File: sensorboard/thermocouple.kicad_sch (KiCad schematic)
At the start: 8 parts, among them U4 MAX31856

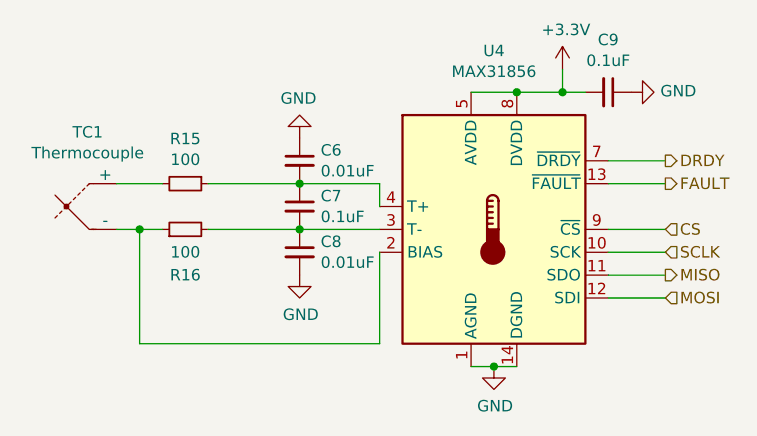
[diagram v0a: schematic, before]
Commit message: Stackup + capacitor fps
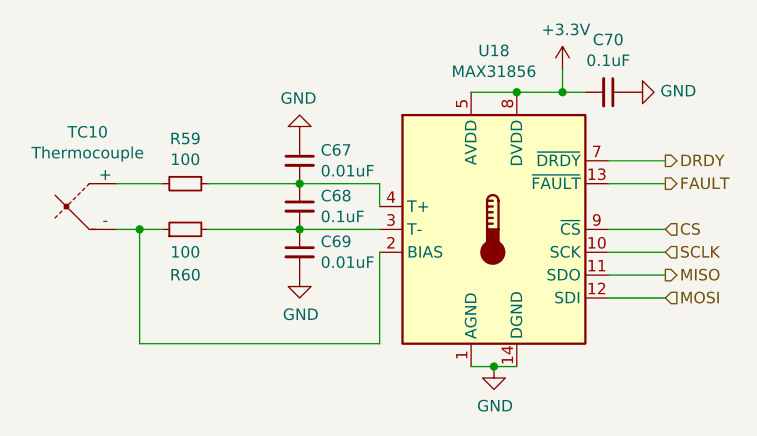
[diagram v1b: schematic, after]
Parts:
- renumbered C6 to C67, C7 to C68, C8 to C69, C9 to C70, R15 to R59, R16 to R60, TC1 to TC10, U4 to U18
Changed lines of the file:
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@@
   (symbol (lib_id "Sensor_Temperature:MAX31856") (at 95.25 73.66 0)
     (in_bom yes) (on_board yes)
-    (property "Reference" "U4" (id 0) (at 95.25 53.8226 0))
+    (property "Reference" "U18" (id 0) (at 95.25 53.8226 0))
     (property "Value" "MAX31856" (id 1) (at 95.25 56.134 0))
     (property "Footprint" "Package_SO:TSSOP-14_4.4x5mm_P0.65mm" (id 2) (at 99.06 87.63 0)
@@
   (symbol (lib_id "power:GND") (at 95.25 88.9 0)
     (in_bom yes) (on_board yes)
-    (property "Reference" "#PWR026" (id 0) (at 95.25 95.25 0)
+    (property "Reference" "#PWR0130" (id 0) (at 95.25 95.25 0)
       (effects (font (size 1.27 1.27)) hide)
     )
@@
   (symbol (lib_id "analogue-cache:+3.3V") (at 102.87 55.88 0)
     (in_bom yes) (on_board yes)
-    (property "Reference" "#PWR028" (id 0) (at 102.87 59.69 0)
+    (property "Reference" "#PWR0131" (id 0) (at 102.87 59.69 0)
       (effects (font (size 1.27 1.27)) hide)
     )
@@
   (symbol (lib_id "Device:C_Small") (at 107.95 58.42 270)
     (in_bom yes) (on_board yes)
-    (property "Reference" "C9" (id 0) (at 107.95 52.6034 90))
+    (property "Reference" "C70" (id 0) (at 107.95 52.6034 90))
     (property "Value" "0.1uF" (id 1) (at 107.95 54.9148 90))
     (property "Footprint" "Capacitor_SMD:C_0603_1608Metric" (id 2) (at 107.95 58.42 0)
@@
   (symbol (lib_id "power:GND") (at 110.49 58.42 90)
     (in_bom yes) (on_board yes)
-    (property "Reference" "#PWR029" (id 0) (at 116.84 58.42 0)
+    (property "Reference" "#PWR0132" (id 0) (at 116.84 58.42 0)
       (effects (font (size 1.27 1.27)) hide)
     )
@@
   (symbol (lib_id "Device:Thermocouple") (at 50.8 71.12 0)
     (in_bom yes) (on_board yes)
-    (property "Reference" "TC1" (id 0) (at 50.1142 62.865 0))
+    (property "Reference" "TC10" (id 0) (at 50.1142 62.865 0))
     (property "Value" "Thermocouple" (id 1) (at 50.1142 65.1764 0))
     (property "Footprint" "TerminalBlock_TE-Connectivity:TerminalBlock_TE_282834-2_1x02_P2.54mm_Horizontal" (id 2) (at 36.195 69.85 0)
@@
   (symbol (lib_id "Device:R_Small") (at 60.96 68.58 270)
     (in_bom yes) (on_board yes)
-    (property "Reference" "R15" (id 0) (at 60.96 63.6016 90))
+    (property "Reference" "R59" (id 0) (at 60.96 63.6016 90))
     (property "Value" "100" (id 1) (at 60.96 65.913 90))
     (property "Footprint" "Resistor_SMD:R_0603_1608Metric" (id 2) (at 60.96 68.58 0)
@@
   (symbol (lib_id "Device:R_Small") (at 60.96 73.66 90)
     (in_bom yes) (on_board yes)
-    (property "Reference" "R16" (id 0) (at 60.96 78.74 90))
+    (property "Reference" "R60" (id 0) (at 60.96 78.74 90))
     (property "Value" "100" (id 1) (at 60.96 76.2 90))
     (property "Footprint" "Resistor_SMD:R_0603_1608Metric" (id 2) (at 60.96 73.66 0)
@@
   (symbol (lib_id "Device:C_Small") (at 73.66 71.12 0)
     (in_bom yes) (on_board yes)
-    (property "Reference" "C7" (id 0) (at 75.9968 69.9516 0)
+    (property "Reference" "C68" (id 0) (at 75.9968 69.9516 0)
       (effects (font (size 1.27 1.27)) (justify left))
     )
@@
   (symbol (lib_id "Device:C_Small") (at 73.66 66.04 0)
     (in_bom yes) (on_board yes)
-    (property "Reference" "C6" (id 0) (at 75.9968 64.8716 0)
+    (property "Reference" "C67" (id 0) (at 75.9968 64.8716 0)
       (effects (font (size 1.27 1.27)) (justify left))
     )
@@
   (symbol (lib_id "Device:C_Small") (at 73.66 76.2 0)
     (in_bom yes) (on_board yes)
-    (property "Reference" "C8" (id 0) (at 75.9968 75.0316 0)
+    (property "Reference" "C69" (id 0) (at 75.9968 75.0316 0)
       (effects (font (size 1.27 1.27)) (justify left))
     )
@@
   (symbol (lib_id "power:GND") (at 73.66 78.74 0)
     (in_bom yes) (on_board yes)
-    (property "Reference" "#PWR025" (id 0) (at 73.66 85.09 0)
+    (property "Reference" "#PWR0129" (id 0) (at 73.66 85.09 0)
       (effects (font (size 1.27 1.27)) hide)
     )
@@
   (symbol (lib_id "power:GND") (at 73.66 63.5 180)
     (in_bom yes) (on_board yes)
-    (property "Reference" "#PWR024" (id 0) (at 73.66 57.15 0)
+    (property "Reference" "#PWR0128" (id 0) (at 73.66 57.15 0)
       (effects (font (size 1.27 1.27)) hide)
     )

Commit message: boost converter fixed
rearrangement of coaxial connector line and gnd stitching
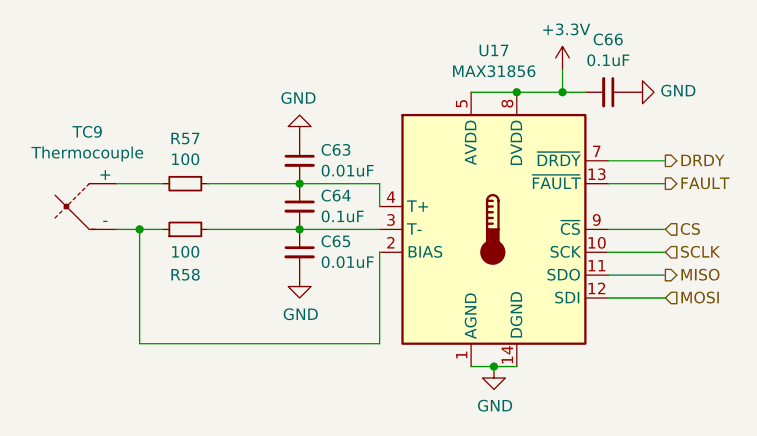
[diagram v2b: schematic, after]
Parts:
- renumbered C67 to C63, C68 to C64, C69 to C65, C70 to C66, R59 to R57, R60 to R58, TC10 to TC9, U18 to U17
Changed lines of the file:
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@@
   (symbol (lib_id "Sensor_Temperature:MAX31856") (at 95.25 73.66 0)
     (in_bom yes) (on_board yes)
-    (property "Reference" "U18" (id 0) (at 95.25 53.8226 0))
+    (property "Reference" "U17" (id 0) (at 95.25 53.8226 0))
     (property "Value" "MAX31856" (id 1) (at 95.25 56.134 0))
     (property "Footprint" "Package_SO:TSSOP-14_4.4x5mm_P0.65mm" (id 2) (at 99.06 87.63 0)
@@
   (symbol (lib_id "power:GND") (at 95.25 88.9 0)
     (in_bom yes) (on_board yes)
-    (property "Reference" "#PWR0130" (id 0) (at 95.25 95.25 0)
+    (property "Reference" "#PWR0125" (id 0) (at 95.25 95.25 0)
       (effects (font (size 1.27 1.27)) hide)
     )
@@
   (symbol (lib_id "analogue-cache:+3.3V") (at 102.87 55.88 0)
     (in_bom yes) (on_board yes)
-    (property "Reference" "#PWR0131" (id 0) (at 102.87 59.69 0)
+    (property "Reference" "#PWR0126" (id 0) (at 102.87 59.69 0)
       (effects (font (size 1.27 1.27)) hide)
     )
@@
   (symbol (lib_id "Device:C_Small") (at 107.95 58.42 270)
     (in_bom yes) (on_board yes)
-    (property "Reference" "C70" (id 0) (at 107.95 52.6034 90))
+    (property "Reference" "C66" (id 0) (at 107.95 52.6034 90))
     (property "Value" "0.1uF" (id 1) (at 107.95 54.9148 90))
     (property "Footprint" "Capacitor_SMD:C_0603_1608Metric" (id 2) (at 107.95 58.42 0)
@@
   (symbol (lib_id "power:GND") (at 110.49 58.42 90)
     (in_bom yes) (on_board yes)
-    (property "Reference" "#PWR0132" (id 0) (at 116.84 58.42 0)
+    (property "Reference" "#PWR0127" (id 0) (at 116.84 58.42 0)
       (effects (font (size 1.27 1.27)) hide)
     )
@@
   (symbol (lib_id "Device:Thermocouple") (at 50.8 71.12 0)
     (in_bom yes) (on_board yes)
-    (property "Reference" "TC10" (id 0) (at 50.1142 62.865 0))
+    (property "Reference" "TC9" (id 0) (at 50.1142 62.865 0))
     (property "Value" "Thermocouple" (id 1) (at 50.1142 65.1764 0))
     (property "Footprint" "TerminalBlock_TE-Connectivity:TerminalBlock_TE_282834-2_1x02_P2.54mm_Horizontal" (id 2) (at 36.195 69.85 0)
@@
   (symbol (lib_id "Device:R_Small") (at 60.96 68.58 270)
     (in_bom yes) (on_board yes)
-    (property "Reference" "R59" (id 0) (at 60.96 63.6016 90))
+    (property "Reference" "R57" (id 0) (at 60.96 63.6016 90))
     (property "Value" "100" (id 1) (at 60.96 65.913 90))
     (property "Footprint" "Resistor_SMD:R_0603_1608Metric" (id 2) (at 60.96 68.58 0)
@@
   (symbol (lib_id "Device:R_Small") (at 60.96 73.66 90)
     (in_bom yes) (on_board yes)
-    (property "Reference" "R60" (id 0) (at 60.96 78.74 90))
+    (property "Reference" "R58" (id 0) (at 60.96 78.74 90))
     (property "Value" "100" (id 1) (at 60.96 76.2 90))
     (property "Footprint" "Resistor_SMD:R_0603_1608Metric" (id 2) (at 60.96 73.66 0)
@@
   (symbol (lib_id "Device:C_Small") (at 73.66 71.12 0)
     (in_bom yes) (on_board yes)
-    (property "Reference" "C68" (id 0) (at 75.9968 69.9516 0)
+    (property "Reference" "C64" (id 0) (at 75.9968 69.9516 0)
       (effects (font (size 1.27 1.27)) (justify left))
     )
@@
   (symbol (lib_id "Device:C_Small") (at 73.66 66.04 0)
     (in_bom yes) (on_board yes)
-    (property "Reference" "C67" (id 0) (at 75.9968 64.8716 0)
+    (property "Reference" "C63" (id 0) (at 75.9968 64.8716 0)
       (effects (font (size 1.27 1.27)) (justify left))
     )
@@
   (symbol (lib_id "Device:C_Small") (at 73.66 76.2 0)
     (in_bom yes) (on_board yes)
-    (property "Reference" "C69" (id 0) (at 75.9968 75.0316 0)
+    (property "Reference" "C65" (id 0) (at 75.9968 75.0316 0)
       (effects (font (size 1.27 1.27)) (justify left))
     )
@@
   (symbol (lib_id "power:GND") (at 73.66 78.74 0)
     (in_bom yes) (on_board yes)
-    (property "Reference" "#PWR0129" (id 0) (at 73.66 85.09 0)
+    (property "Reference" "#PWR0124" (id 0) (at 73.66 85.09 0)
       (effects (font (size 1.27 1.27)) hide)
     )
@@
   (symbol (lib_id "power:GND") (at 73.66 63.5 180)
     (in_bom yes) (on_board yes)
-    (property "Reference" "#PWR0128" (id 0) (at 73.66 57.15 0)
+    (property "Reference" "#PWR0123" (id 0) (at 73.66 57.15 0)
       (effects (font (size 1.27 1.27)) hide)
     )

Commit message: Changed pins for CAN lines and removed LED
need to rearrange LNA_IN line for less interference
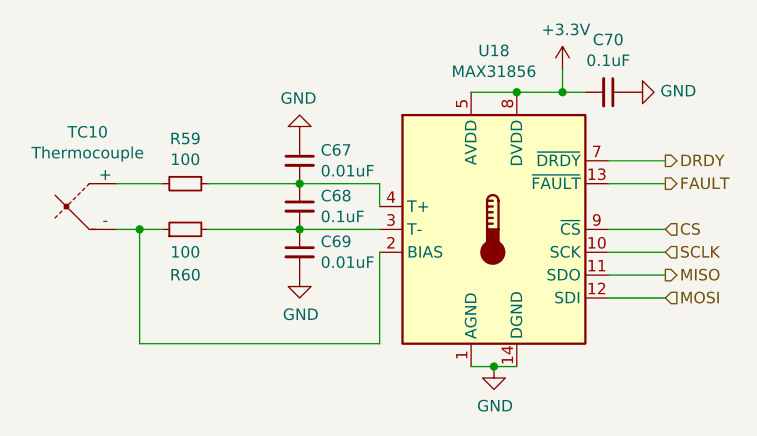
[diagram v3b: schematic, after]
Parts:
- renumbered C63 to C67, C64 to C68, C65 to C69, C66 to C70, R57 to R59, R58 to R60, TC9 to TC10, U17 to U18
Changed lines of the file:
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@@
   (symbol (lib_id "Sensor_Temperature:MAX31856") (at 95.25 73.66 0)
     (in_bom yes) (on_board yes)
-    (property "Reference" "U17" (id 0) (at 95.25 53.8226 0))
+    (property "Reference" "U18" (id 0) (at 95.25 53.8226 0))
     (property "Value" "MAX31856" (id 1) (at 95.25 56.134 0))
     (property "Footprint" "Package_SO:TSSOP-14_4.4x5mm_P0.65mm" (id 2) (at 99.06 87.63 0)
@@
   (symbol (lib_id "power:GND") (at 95.25 88.9 0)
     (in_bom yes) (on_board yes)
-    (property "Reference" "#PWR0125" (id 0) (at 95.25 95.25 0)
+    (property "Reference" "#PWR0130" (id 0) (at 95.25 95.25 0)
       (effects (font (size 1.27 1.27)) hide)
     )
@@
   (symbol (lib_id "analogue-cache:+3.3V") (at 102.87 55.88 0)
     (in_bom yes) (on_board yes)
-    (property "Reference" "#PWR0126" (id 0) (at 102.87 59.69 0)
+    (property "Reference" "#PWR0131" (id 0) (at 102.87 59.69 0)
       (effects (font (size 1.27 1.27)) hide)
     )
@@
   (symbol (lib_id "Device:C_Small") (at 107.95 58.42 270)
     (in_bom yes) (on_board yes)
-    (property "Reference" "C66" (id 0) (at 107.95 52.6034 90))
+    (property "Reference" "C70" (id 0) (at 107.95 52.6034 90))
     (property "Value" "0.1uF" (id 1) (at 107.95 54.9148 90))
     (property "Footprint" "Capacitor_SMD:C_0603_1608Metric" (id 2) (at 107.95 58.42 0)
@@
   (symbol (lib_id "power:GND") (at 110.49 58.42 90)
     (in_bom yes) (on_board yes)
-    (property "Reference" "#PWR0127" (id 0) (at 116.84 58.42 0)
+    (property "Reference" "#PWR0132" (id 0) (at 116.84 58.42 0)
       (effects (font (size 1.27 1.27)) hide)
     )
@@
   (symbol (lib_id "Device:Thermocouple") (at 50.8 71.12 0)
     (in_bom yes) (on_board yes)
-    (property "Reference" "TC9" (id 0) (at 50.1142 62.865 0))
+    (property "Reference" "TC10" (id 0) (at 50.1142 62.865 0))
     (property "Value" "Thermocouple" (id 1) (at 50.1142 65.1764 0))
     (property "Footprint" "TerminalBlock_TE-Connectivity:TerminalBlock_TE_282834-2_1x02_P2.54mm_Horizontal" (id 2) (at 36.195 69.85 0)
@@
   (symbol (lib_id "Device:R_Small") (at 60.96 68.58 270)
     (in_bom yes) (on_board yes)
-    (property "Reference" "R57" (id 0) (at 60.96 63.6016 90))
+    (property "Reference" "R59" (id 0) (at 60.96 63.6016 90))
     (property "Value" "100" (id 1) (at 60.96 65.913 90))
     (property "Footprint" "Resistor_SMD:R_0603_1608Metric" (id 2) (at 60.96 68.58 0)
@@
   (symbol (lib_id "Device:R_Small") (at 60.96 73.66 90)
     (in_bom yes) (on_board yes)
-    (property "Reference" "R58" (id 0) (at 60.96 78.74 90))
+    (property "Reference" "R60" (id 0) (at 60.96 78.74 90))
     (property "Value" "100" (id 1) (at 60.96 76.2 90))
     (property "Footprint" "Resistor_SMD:R_0603_1608Metric" (id 2) (at 60.96 73.66 0)
@@
   (symbol (lib_id "Device:C_Small") (at 73.66 71.12 0)
     (in_bom yes) (on_board yes)
-    (property "Reference" "C64" (id 0) (at 75.9968 69.9516 0)
+    (property "Reference" "C68" (id 0) (at 75.9968 69.9516 0)
       (effects (font (size 1.27 1.27)) (justify left))
     )
@@
   (symbol (lib_id "Device:C_Small") (at 73.66 66.04 0)
     (in_bom yes) (on_board yes)
-    (property "Reference" "C63" (id 0) (at 75.9968 64.8716 0)
+    (property "Reference" "C67" (id 0) (at 75.9968 64.8716 0)
       (effects (font (size 1.27 1.27)) (justify left))
     )
@@
   (symbol (lib_id "Device:C_Small") (at 73.66 76.2 0)
     (in_bom yes) (on_board yes)
-    (property "Reference" "C65" (id 0) (at 75.9968 75.0316 0)
+    (property "Reference" "C69" (id 0) (at 75.9968 75.0316 0)
       (effects (font (size 1.27 1.27)) (justify left))
     )
@@
   (symbol (lib_id "power:GND") (at 73.66 78.74 0)
     (in_bom yes) (on_board yes)
-    (property "Reference" "#PWR0124" (id 0) (at 73.66 85.09 0)
+    (property "Reference" "#PWR0129" (id 0) (at 73.66 85.09 0)
       (effects (font (size 1.27 1.27)) hide)
     )
@@
   (symbol (lib_id "power:GND") (at 73.66 63.5 180)
     (in_bom yes) (on_board yes)
-    (property "Reference" "#PWR0123" (id 0) (at 73.66 57.15 0)
+    (property "Reference" "#PWR0128" (id 0) (at 73.66 57.15 0)
       (effects (font (size 1.27 1.27)) hide)
     )

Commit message: rearrange CAN, USB port and new copies
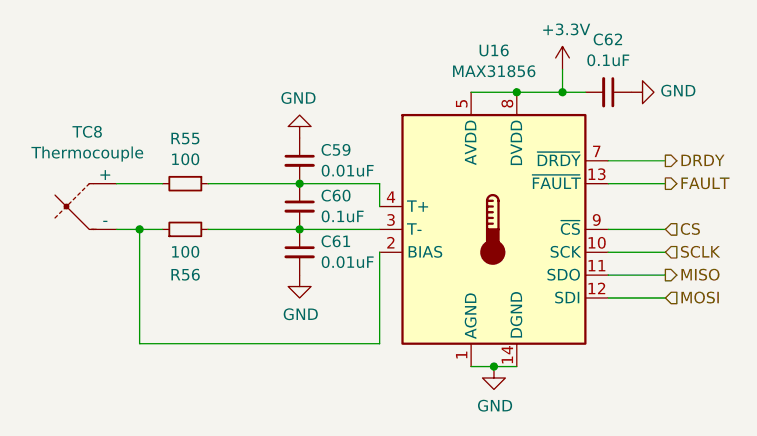
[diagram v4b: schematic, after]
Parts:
- renumbered C67 to C59, C68 to C60, C69 to C61, C70 to C62, R59 to R55, R60 to R56, TC10 to TC8, U18 to U16
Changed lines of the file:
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@@
   (symbol (lib_id "Sensor_Temperature:MAX31856") (at 95.25 73.66 0)
     (in_bom yes) (on_board yes)
-    (property "Reference" "U18" (id 0) (at 95.25 53.8226 0))
+    (property "Reference" "U16" (id 0) (at 95.25 53.8226 0))
     (property "Value" "MAX31856" (id 1) (at 95.25 56.134 0))
     (property "Footprint" "Package_SO:TSSOP-14_4.4x5mm_P0.65mm" (id 2) (at 99.06 87.63 0)
@@
   (symbol (lib_id "power:GND") (at 95.25 88.9 0)
     (in_bom yes) (on_board yes)
-    (property "Reference" "#PWR0130" (id 0) (at 95.25 95.25 0)
+    (property "Reference" "#PWR0120" (id 0) (at 95.25 95.25 0)
       (effects (font (size 1.27 1.27)) hide)
     )
@@
   (symbol (lib_id "analogue-cache:+3.3V") (at 102.87 55.88 0)
     (in_bom yes) (on_board yes)
-    (property "Reference" "#PWR0131" (id 0) (at 102.87 59.69 0)
+    (property "Reference" "#PWR0121" (id 0) (at 102.87 59.69 0)
       (effects (font (size 1.27 1.27)) hide)
     )
@@
   (symbol (lib_id "Device:C_Small") (at 107.95 58.42 270)
     (in_bom yes) (on_board yes)
-    (property "Reference" "C70" (id 0) (at 107.95 52.6034 90))
+    (property "Reference" "C62" (id 0) (at 107.95 52.6034 90))
     (property "Value" "0.1uF" (id 1) (at 107.95 54.9148 90))
     (property "Footprint" "Capacitor_SMD:C_0603_1608Metric" (id 2) (at 107.95 58.42 0)
@@
   (symbol (lib_id "power:GND") (at 110.49 58.42 90)
     (in_bom yes) (on_board yes)
-    (property "Reference" "#PWR0132" (id 0) (at 116.84 58.42 0)
+    (property "Reference" "#PWR0122" (id 0) (at 116.84 58.42 0)
       (effects (font (size 1.27 1.27)) hide)
     )
@@
   (symbol (lib_id "Device:Thermocouple") (at 50.8 71.12 0)
     (in_bom yes) (on_board yes)
-    (property "Reference" "TC10" (id 0) (at 50.1142 62.865 0))
+    (property "Reference" "TC8" (id 0) (at 50.1142 62.865 0))
     (property "Value" "Thermocouple" (id 1) (at 50.1142 65.1764 0))
     (property "Footprint" "TerminalBlock_TE-Connectivity:TerminalBlock_TE_282834-2_1x02_P2.54mm_Horizontal" (id 2) (at 36.195 69.85 0)
@@
   (symbol (lib_id "Device:R_Small") (at 60.96 68.58 270)
     (in_bom yes) (on_board yes)
-    (property "Reference" "R59" (id 0) (at 60.96 63.6016 90))
+    (property "Reference" "R55" (id 0) (at 60.96 63.6016 90))
     (property "Value" "100" (id 1) (at 60.96 65.913 90))
     (property "Footprint" "Resistor_SMD:R_0603_1608Metric" (id 2) (at 60.96 68.58 0)
@@
   (symbol (lib_id "Device:R_Small") (at 60.96 73.66 90)
     (in_bom yes) (on_board yes)
-    (property "Reference" "R60" (id 0) (at 60.96 78.74 90))
+    (property "Reference" "R56" (id 0) (at 60.96 78.74 90))
     (property "Value" "100" (id 1) (at 60.96 76.2 90))
     (property "Footprint" "Resistor_SMD:R_0603_1608Metric" (id 2) (at 60.96 73.66 0)
@@
   (symbol (lib_id "Device:C_Small") (at 73.66 71.12 0)
     (in_bom yes) (on_board yes)
-    (property "Reference" "C68" (id 0) (at 75.9968 69.9516 0)
+    (property "Reference" "C60" (id 0) (at 75.9968 69.9516 0)
       (effects (font (size 1.27 1.27)) (justify left))
     )
@@
   (symbol (lib_id "Device:C_Small") (at 73.66 66.04 0)
     (in_bom yes) (on_board yes)
-    (property "Reference" "C67" (id 0) (at 75.9968 64.8716 0)
+    (property "Reference" "C59" (id 0) (at 75.9968 64.8716 0)
       (effects (font (size 1.27 1.27)) (justify left))
     )
@@
   (symbol (lib_id "Device:C_Small") (at 73.66 76.2 0)
     (in_bom yes) (on_board yes)
-    (property "Reference" "C69" (id 0) (at 75.9968 75.0316 0)
+    (property "Reference" "C61" (id 0) (at 75.9968 75.0316 0)
       (effects (font (size 1.27 1.27)) (justify left))
     )
@@
   (symbol (lib_id "power:GND") (at 73.66 78.74 0)
     (in_bom yes) (on_board yes)
-    (property "Reference" "#PWR0129" (id 0) (at 73.66 85.09 0)
+    (property "Reference" "#PWR0119" (id 0) (at 73.66 85.09 0)
       (effects (font (size 1.27 1.27)) hide)
     )
@@
   (symbol (lib_id "power:GND") (at 73.66 63.5 180)
     (in_bom yes) (on_board yes)
-    (property "Reference" "#PWR0128" (id 0) (at 73.66 57.15 0)
+    (property "Reference" "#PWR0118" (id 0) (at 73.66 57.15 0)
       (effects (font (size 1.27 1.27)) hide)
     )
